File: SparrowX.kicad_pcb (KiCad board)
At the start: 4 copper layers, 31.6 x 26.6 mm, 25 parts, among them J1 NORTH, J2 SOUTH, J3 WEST, J4 EAST, U1 TPS629210-Q1, U2 LD49100PU33RY, U3 STM32G0B1CBU6, U4 TCAN332G, U5 TCAN332G

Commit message: Routing tweaks
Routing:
- net GND: track 12.0 -> 14.7 mm, vias 80 -> 82
- net /PB15: track 18.1 -> 19.9 mm
- net /PB2: track 18.2 -> 19.8 mm

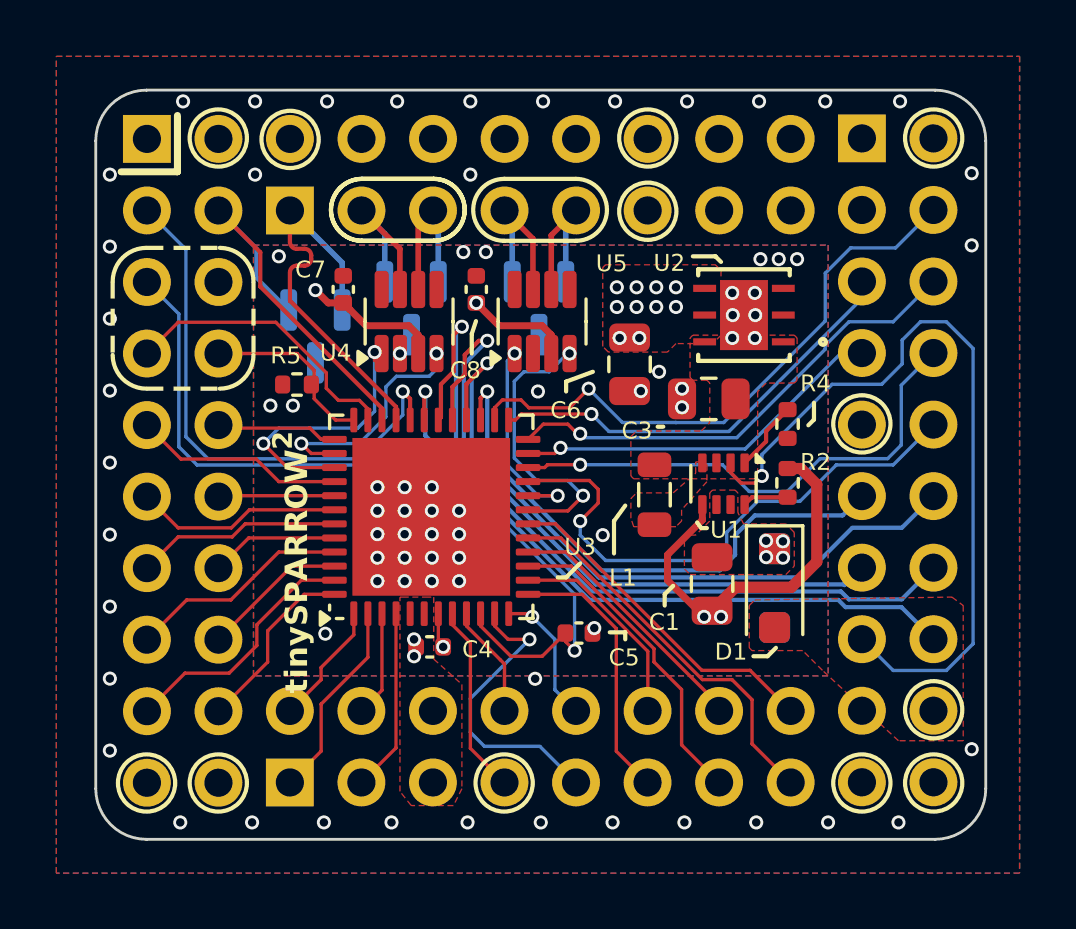
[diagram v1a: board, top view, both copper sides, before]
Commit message: Add VREF+ RC-filter; silkscreen adjustments
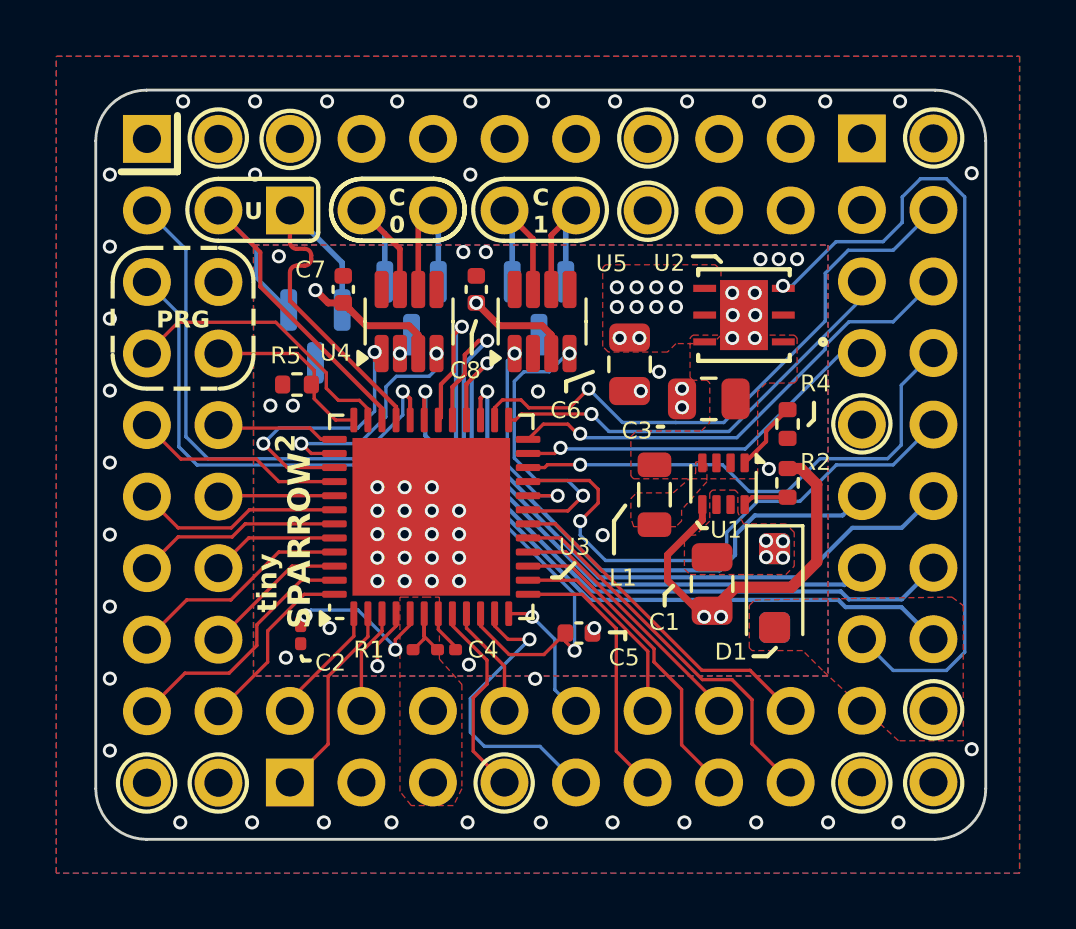
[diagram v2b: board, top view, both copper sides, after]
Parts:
- added C2: 0.1 uF, Capacitor_SMD:C_0201_0603Metric, F.Cu at (161.9, 100.1)
- added R1: 10, Resistor_SMD:R_0201_0603Metric, F.Cu at (165.5, 100.7)
- C4: footprint Capacitor_SMD:C_0402_1005Metric -> Capacitor_SMD:C_0201_0603Metric
- moved C4 0.61 mm to (167.1, 100.7)
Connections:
- J4 pad 15: /P_{GOOD} -> /PG_{LR}
- U1 pad 2: /P_{GOOD} -> /PG_{SWR}
- U2 pad 3: unconnected-(U2-PG-Pad3) -> /PG_{LR}
- U3 pad 5: +3V3 -> /VREF
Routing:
- net /PG_{LR}: track 0.00 -> 29.5 mm, vias 0 -> 1
- net /P_{GOOD}: track 28.1 -> 0.00 mm, vias 1 -> 0
- net /VREF: track 0.00 -> 5.83 mm, vias 0 -> 2
- net +3V3: track 8.76 -> 11.7 mm, vias 14 -> 12
- net /VBAT: track 6.50 -> 7.84 mm, vias 0 -> 1
- net GND: track 14.7 -> 15.0 mm, vias 82 -> 83
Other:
- board text added: "C 0"
- board text added: "C 1"
- board text added: "PRG"
- board text added: "SPARROW"
- board text added: "U"
- board text added: "tiny"
- board text removed: "tinySPARROW"

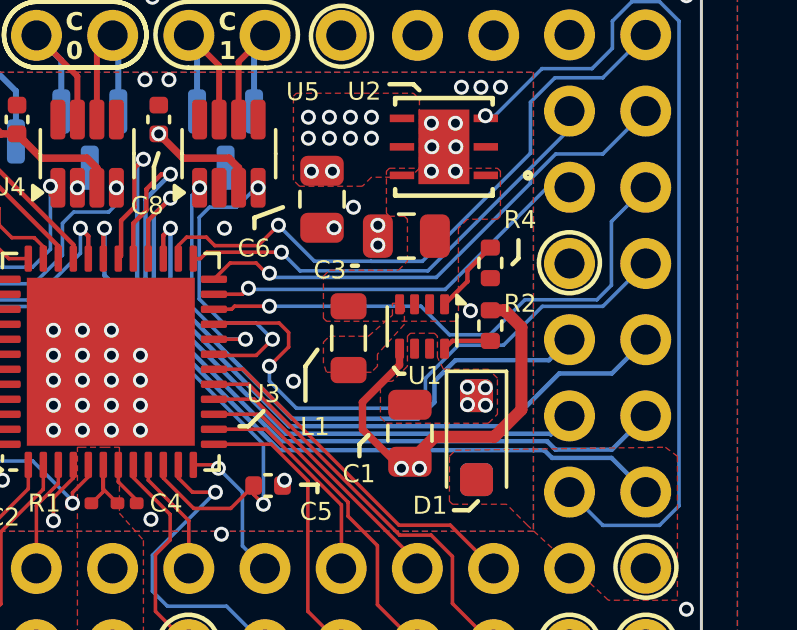
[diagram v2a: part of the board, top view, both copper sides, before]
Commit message: Tie power good pin of TPS629210 to GND (see datasheet section 8.3.5)
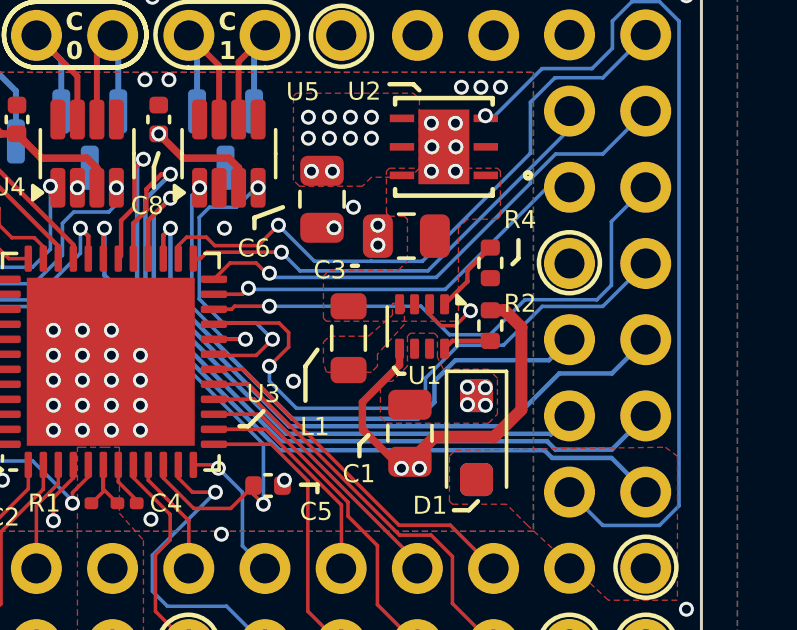
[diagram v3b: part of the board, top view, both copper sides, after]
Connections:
- U1 pad 2: /PG_{SWR} -> GND
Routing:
- net GND: track 15.0 -> 17.1 mm
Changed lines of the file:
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@@
 	(net 73 "/VREF")
 	(net 74 "/PG_{LR}")
-	(net 75 "/PG_{SWR}")
 	(footprint "Capacitor_SMD:C_0402_1005Metric"
 		(layer "F.Cu")
@@
 		(tags "resistor")
 		(property "Reference" "R1"
-			(at 1.250001 0 360)
+			(at 1.250001 0 0)
 			(layer "F.SilkS")
 			(effects
@@
 		)
 		(property "Value" "10"
-			(at 0 1.05 360)
+			(at 0 1.05 0)
 			(layer "F.Fab")
 			(effects
@@
 		)
 		(fp_text user "${REFERENCE}"
-			(at 0 -0.680001 360)
+			(at 0 -0.680001 0)
 			(layer "F.Fab")
 			(effects
@@
 		(tags "capacitor")
 		(property "Reference" "C2"
-			(at 0.9978 -1.060001 360)
+			(at 0.9978 -1.060001 0)
 			(layer "F.SilkS")
 			(effects
@@
 			(layers "F.Cu" "F.Paste" "F.Mask")
 			(roundrect_rratio 0.1666666667)
-			(net 75 "/PG_{SWR}")
+			(net 1 "GND")
 			(pinfunction "PG")
-			(pintype "output+no_connect")
+			(pintype "output")
 			(thermal_bridge_angle 45)
 		)
@@
 	)
 	(segment
+		(start 177.1378 94.0348)
+		(end 177.1378 94.3698)
+		(width 0.12)
+		(layer "F.Cu")
+		(net 1)
+	)
+	(segment
 		(start 166.762136 99.387764)
 		(end 166.762136 99.952648)
@@
 	)
 	(segment
+		(start 177.1378 94.3698)
+		(end 177.518 94.75)
+		(width 0.12)
+		(layer "F.Cu")
+		(net 1)
+	)
+	(segment
 		(start 176.1378 96.0622)
 		(end 174.9 97.3)
@@
 	)
 	(segment
+		(start 178 94.75)
+		(end 178.5 94.25)
+		(width 0.12)
+		(layer "F.Cu")
+		(net 1)
+	)
+	(segment
 		(start 176.1378 95.5148)
 		(end 176.1378 96.0622)
@@
 		(layer "F.Cu")
 		(net 1)
+	)
+	(segment
+		(start 177.518 94.75)
+		(end 178 94.75)
+		(width 0.12)
+		(layer "F.Cu")
+		(net 1)

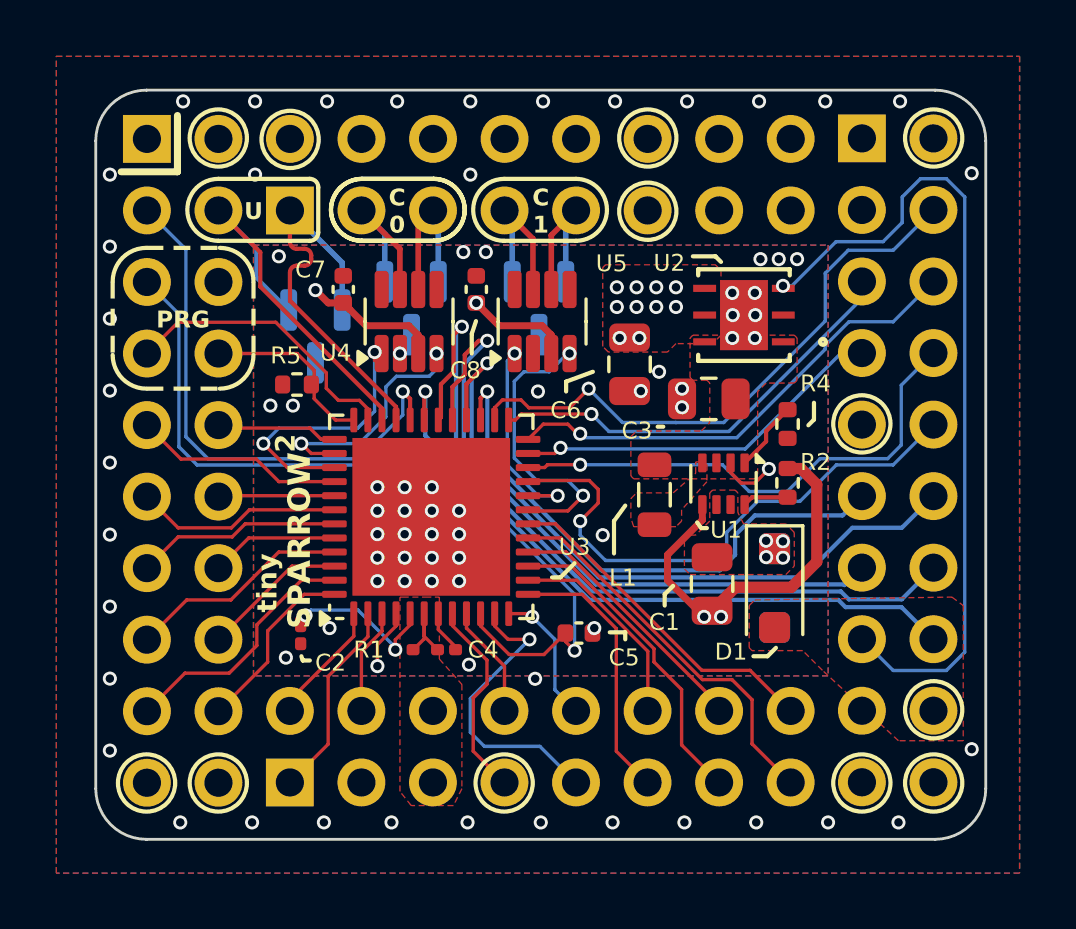
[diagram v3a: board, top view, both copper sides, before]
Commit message: WIP: new switching regulator
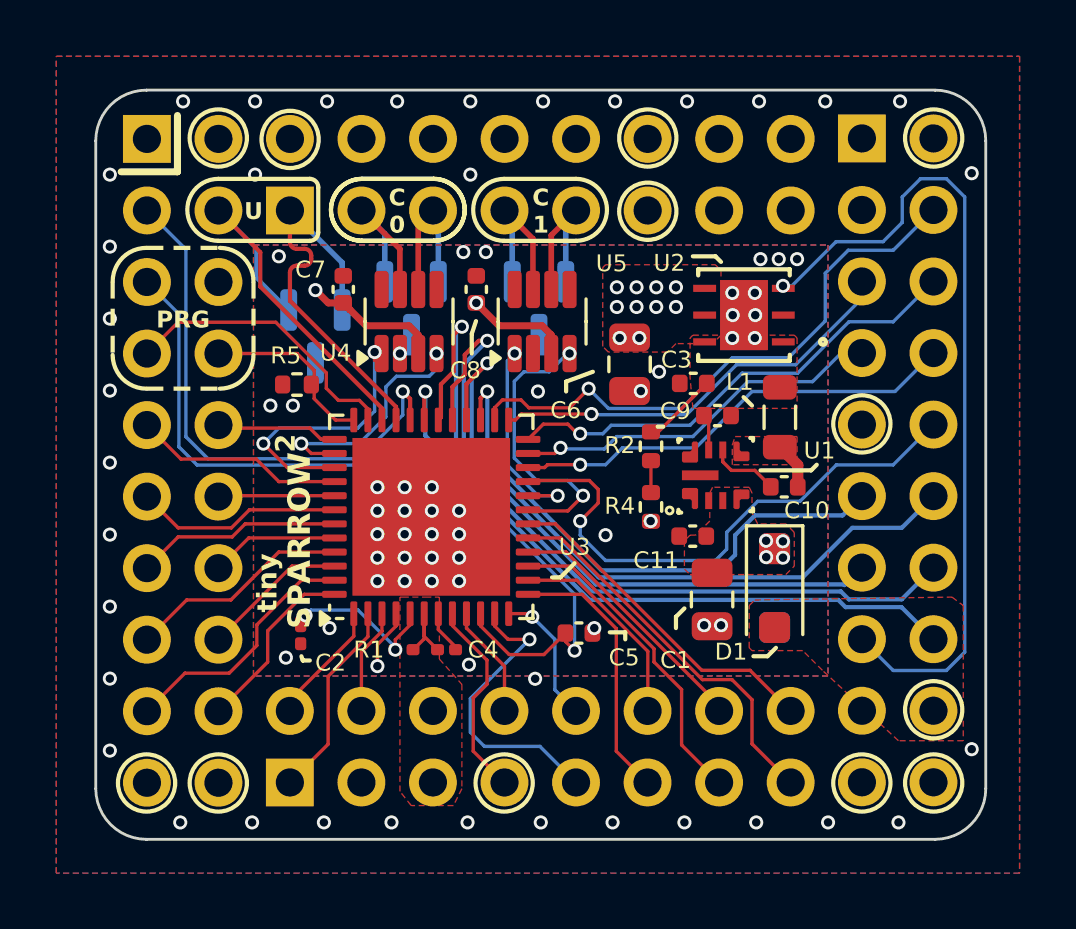
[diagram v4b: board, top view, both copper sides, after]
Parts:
- added C10: 0.1 uF, Capacitor_SMD:C_0402_1005Metric, F.Cu at (179.0, 94.9)
- added C11: 0.1 uF, Capacitor_SMD:C_0402_1005Metric, F.Cu at (175.8, 96.6)
- added C9: 1uF, Capacitor_SMD:C_0402_1005Metric, F.Cu at (176.7, 92.4)
- C3: footprint Capacitor_SMD:C_0805_2012Metric -> Capacitor_SMD:C_0402_1005Metric
- D5: value SMF16A -> SMF26A
- R2: value 27.4K -> 33.2K
- R4: value 64.9K -> 14.3K
- U1: value TPS629210-Q1 -> LMR43610MSC3RPERQ1; footprint Package_TO_SOT_SMD:SOT-583-8 -> footprint:RPE0009A-MFG
- moved R4 5.67 mm to (174.3, 95.6)
- moved L1 5.23 mm to (178.9, 92.4)
- moved R2 5.02 mm to (174.3, 93.4)
- moved C3 0.78 mm to (175.8, 91.2)
- moved C1 0.55 mm to (176.5, 98.9)
- moved U1 0.41 mm to (176.6, 94.5), turned to 90 degrees
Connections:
- R2 pad 1: Net-(U1-MODE) -> Net-(U1-VOUT_FB)
- R2 pad 2: GND -> /3V_{PF}
- R4 pad 1: Net-(U1-FB/VSET) -> Net-(U1-VOUT_FB)
- U1 pad 1: Net-(U1-FB/VSET) -> GND
- U1 pad 3: /3V_{PF} -> VDC_{PROTECTED}
- U1 pad 4: /SW -> VDC_{PROTECTED}
- U1 pad 5: GND -> /SW
- U1 pad 6: VDC_{PROTECTED} -> Net-(U1-BOOT)
- U1 pad 7: VDC_{PROTECTED} -> Net-(U1-VCC)
- U1 pad 8: Net-(U1-MODE) -> Net-(U1-VOUT_FB)
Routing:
- net GND: track 17.1 -> 1.53 mm, vias 83 -> 81
- net /3V_{PF}: track 0.00 -> 2.70 mm
- net Net-(U1-FB/VSET): track 2.52 -> 0.00 mm
- net Net-(U1-BOOT): track 0.00 -> 2.50 mm
- net /PB10: track 18.1 -> 16.1 mm
- net /SW: track 0.00 -> 1.67 mm
- net Net-(U1-MODE): track 1.63 -> 0.00 mm
- net Net-(U1-VCC): track 0.00 -> 1.29 mm
- net Net-(U1-VOUT_FB): track 0.00 -> 1.13 mm

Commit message: PSU P1 migration done!
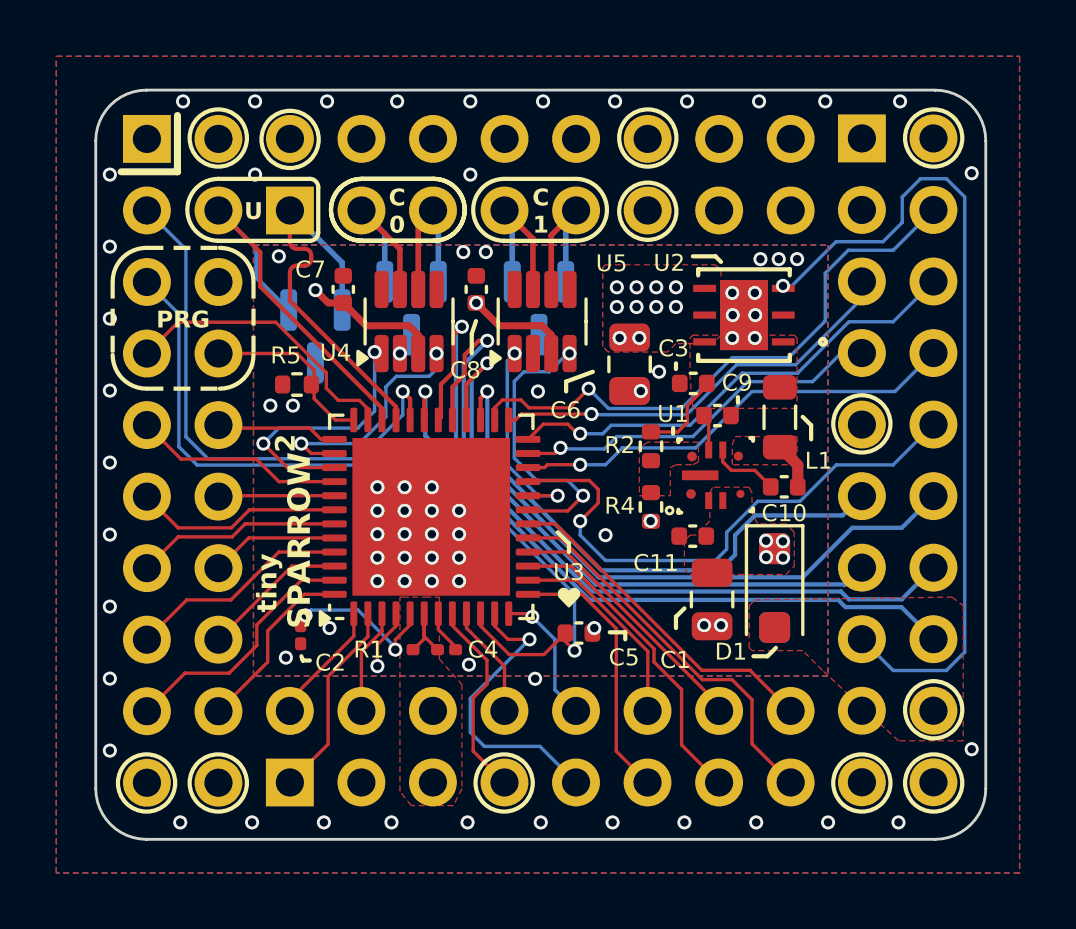
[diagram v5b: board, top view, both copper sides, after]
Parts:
- added G***: LOGO, LOGO, F.Cu at (171.4, 98.8)
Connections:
- net Net-(U1-VOUT_FB) renamed /VFB
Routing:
- net /VFB: track 1.13 -> 0.00 mm
- added copper zone on F.Cu, net /VFB

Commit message: Via tweaks
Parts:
- R2: value 33.2K -> 38K
- R4: value 14.3K -> 12K
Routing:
- net /PB2: track 19.8 -> 18.7 mm
- net /PB10: track 16.1 -> 16.9 mm
- net GND: vias 81 -> 91

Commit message: Give USB some solid ground underneath
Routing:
- net +3V3: track 11.7 -> 39.4 mm
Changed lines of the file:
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@@
 		(tags "resistor")
 		(property "Reference" "R4"
-			(at -0.0376 1.108 360)
+			(at -0.0376 1.108 0)
 			(layer "F.SilkS")
 			(effects
@@
 	)
 	(segment
+		(start 158.438433 96.5218)
+		(end 157.6662 95.749567)
+		(width 0.4)
+		(layer "In1.Cu")
+		(net 2)
+	)
+	(segment
+		(start 165.4 99.4)
+		(end 164.1 99.4)
+		(width 0.4)
+		(layer "In1.Cu")
+		(net 2)
+	)
+	(segment
+		(start 161.2218 96.5218)
+		(end 158.438433 96.5218)
+		(width 0.4)
+		(layer "In1.Cu")
+		(net 2)
+	)
+	(segment
+		(start 162.855201 88.355201)
+		(end 168.110532 88.355201)
+		(width 0.25)
+		(layer "In1.Cu")
+		(net 2)
+	)
+	(segment
+		(start 166.5716 100.5716)
+		(end 165.4 99.4)
+		(width 0.4)
+		(layer "In1.Cu")
+		(net 2)
+	)
+	(segment
+		(start 166.5716 102.8408)
+		(end 166.5716 100.5716)
+		(width 0.4)
+		(layer "In1.Cu")
+		(net 2)
+	)
+	(segment
+		(start 164.1 99.4)
+		(end 161.2218 96.5218)
+		(width 0.4)
+		(layer "In1.Cu")
+		(net 2)
+	)
+	(segment
+		(start 157.6662 95.749567)
+		(end 157.6662 88.9018)
+		(width 0.4)
+		(layer "In1.Cu")
+		(net 2)
+	)
+	(segment
+		(start 157.6662 88.9018)
+		(end 158.9562 87.6118)
+		(width 0.4)
+		(layer "In1.Cu")
+		(net 2)
+	)
+	(segment
+		(start 162.4 87.9)
+		(end 162.855201 88.355201)
+		(width 0.25)
+		(layer "In1.Cu")
+		(net 2)
+	)
+	(segment
 		(start 168.262136 99.387764)
 		(end 168.262136 99.825263)
@@
 		(polygon
 			(pts
-				(xy 173 110) (xy 173 91.5) (xy 191 91.5) (xy 191 110)
+				(xy 174.4 110) (xy 174.4 91.5) (xy 191 91.5) (xy 191 110)
 			)
 		)
@@
 		(polygon
 			(pts
-				(xy 180.5 86) (xy 149.5 86) (xy 149.5 74.3) (xy 180.5 74.3)
+				(xy 180.4 87.4) (xy 149.4 87.4) (xy 149.5 74.3) (xy 180.5 74.3)
 			)
 		)
@@
 		(polygon
 			(pts
-				(xy 157.1 86) (xy 157.1 111) (xy 149.3 111) (xy 149.3 86)
-			)
-		)
-	)
-	(zone
-		(net 2)
-		(net_name "+3V3")
-		(layer "In1.Cu")
-		(name "3V3_THERMAL")
-		(hatch edge 0.5)
-		(priority 2)
-		(connect_pads
-			(clearance 0.25)
-		)
-		(min_thickness 0.1)
-		(filled_areas_thickness no)
-		(fill yes
-			(thermal_gap 0.3)
-			(thermal_bridge_width 0.3)
-		)
-		(polygon
-			(pts
-				(xy 161.05 89.4) (xy 157.55 89.4) (xy 157.55 86) (xy 161.05 86)
+				(xy 164.1 85.8) (xy 164.1 110.8) (xy 149.3 110.8) (xy 149.3 85.8)
 			)
 		)
